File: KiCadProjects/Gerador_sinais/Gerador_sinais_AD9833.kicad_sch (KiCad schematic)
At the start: 18 parts, among them J1 tensoes, J3 sinais analogicos, J4 comunicacao / sinais digitais, J6 pinos de prova, SW1 botao_forma_onda, SW2 botao_incremento_freq, SW3 botao_decremento_freq, SW4 botao_save_Rgain, SW5 botao_aumenta_Rgain, SW6 botao_diminui_Rgain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

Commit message: Atualização das informações da página do esquemático
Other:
- title: Gerador de sinais AD9833 ganho BIA -> Gerador de sinais AD9833
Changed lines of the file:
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@@
   (paper "A4")
   (title_block
-    (title "Gerador de sinais AD9833 ganho BIA")
-    (date "2023-04-19")
+    (title "Gerador de sinais AD9833")
+    (date "2023-07-12")
     (rev "v01")
     (company "EITduino")
     (comment 1 "Autor: Gustavo Pinheiro")
     (comment 2 "placa de face simples 90x100 mm")
-    (comment 3 "Gerador de sinais implementado para a balanca de bioimpedancia")
+    (comment 3 "Gerador de sinais")
     (comment 4 "potenciometro digital: x9c104 (100k)")
-    (comment 5 "controle do pot dig: https://drive.google.com/drive/folders/1YxCH3byESSoGbQtQ7U2HApApApZmV-oW")
   )
   (junction (at 128.905 53.34) (diameter 0) (color 0 0 0 0)

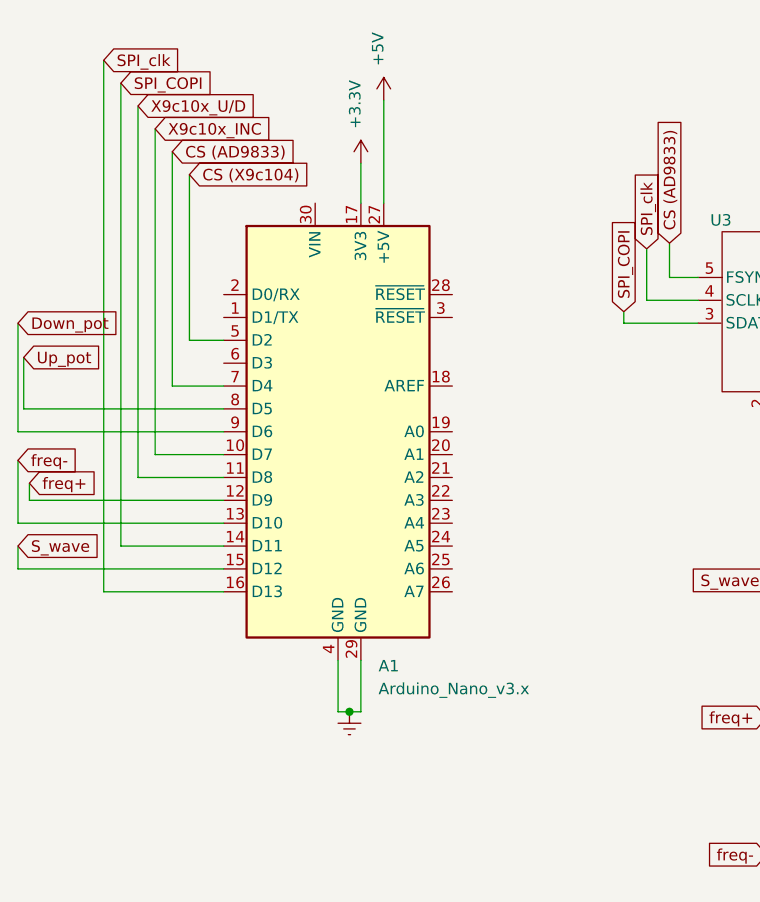
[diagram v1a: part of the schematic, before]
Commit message: Conexão do arduino nano ao I2c 1
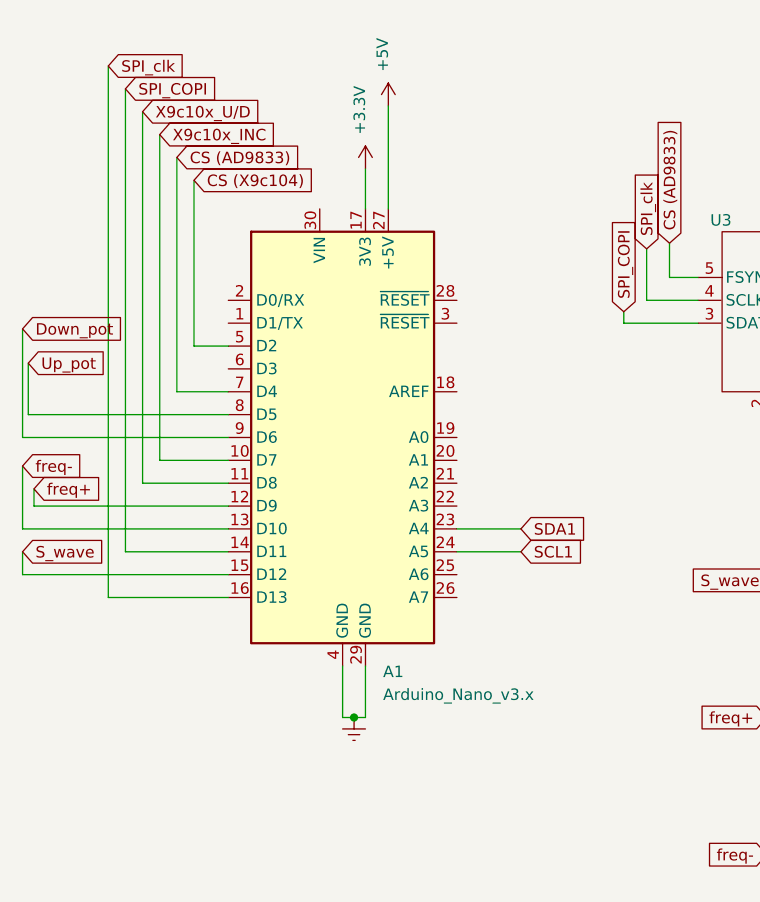
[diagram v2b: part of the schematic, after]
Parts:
- Rpulldown_pot1: footprint (none) -> Resistor_THT:R_Axial_DIN0204_L3.6mm_D1.6mm_P5.08mm_Horizontal
- SW1, SW2, SW3, SW4, SW5, SW6: footprint (none) -> push_button_2_pin:SW_BUTT-2
- U2: footprint (none) -> X9c10X_module:X9c10X_module
- U3: footprint (none) -> AD9833_module:AD9833_module
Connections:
- net SCL1: now also A1.24 (A5)
- net SDA1: now also A1.23 (A4)
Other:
- moved on the sheet: A1

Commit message: mudancas comunicacao SPI
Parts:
- removed Rpulldown_pot1: 10k, Resistor_THT:R_Axial_DIN0204_L3.6mm_D1.6mm_P5.08mm_Horizontal, symbol Device:R
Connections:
- net +3.3V: no longer A1.17 (3V3)
- net +5V: no longer SW4.1
- net CS (X9c104): no longer SW4.2
- net Earth: now also SW4.2
- net storage_R: now reaches A1.6 (D3)
- net storage_R: now also SW4.1

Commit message: Atribuição dos footprints
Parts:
- U1: footprint footprints:N_8_ADI -> AD828AN:N_8_ADI
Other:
- moved on the sheet: A1

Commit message: Atribuição dos footprints
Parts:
- U1: footprint AD828AN:N_8_ADI -> AD828:N_8_ADI
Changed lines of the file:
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@@
       (effects (font (size 1.524 1.524)))
     )
-    (property "Footprint" "AD828AN:N_8_ADI" (at 177.165 45.085 0)
+    (property "Footprint" "AD828:N_8_ADI" (at 177.165 45.085 0)
       (effects (font (size 1.27 1.27) italic) hide)
     )

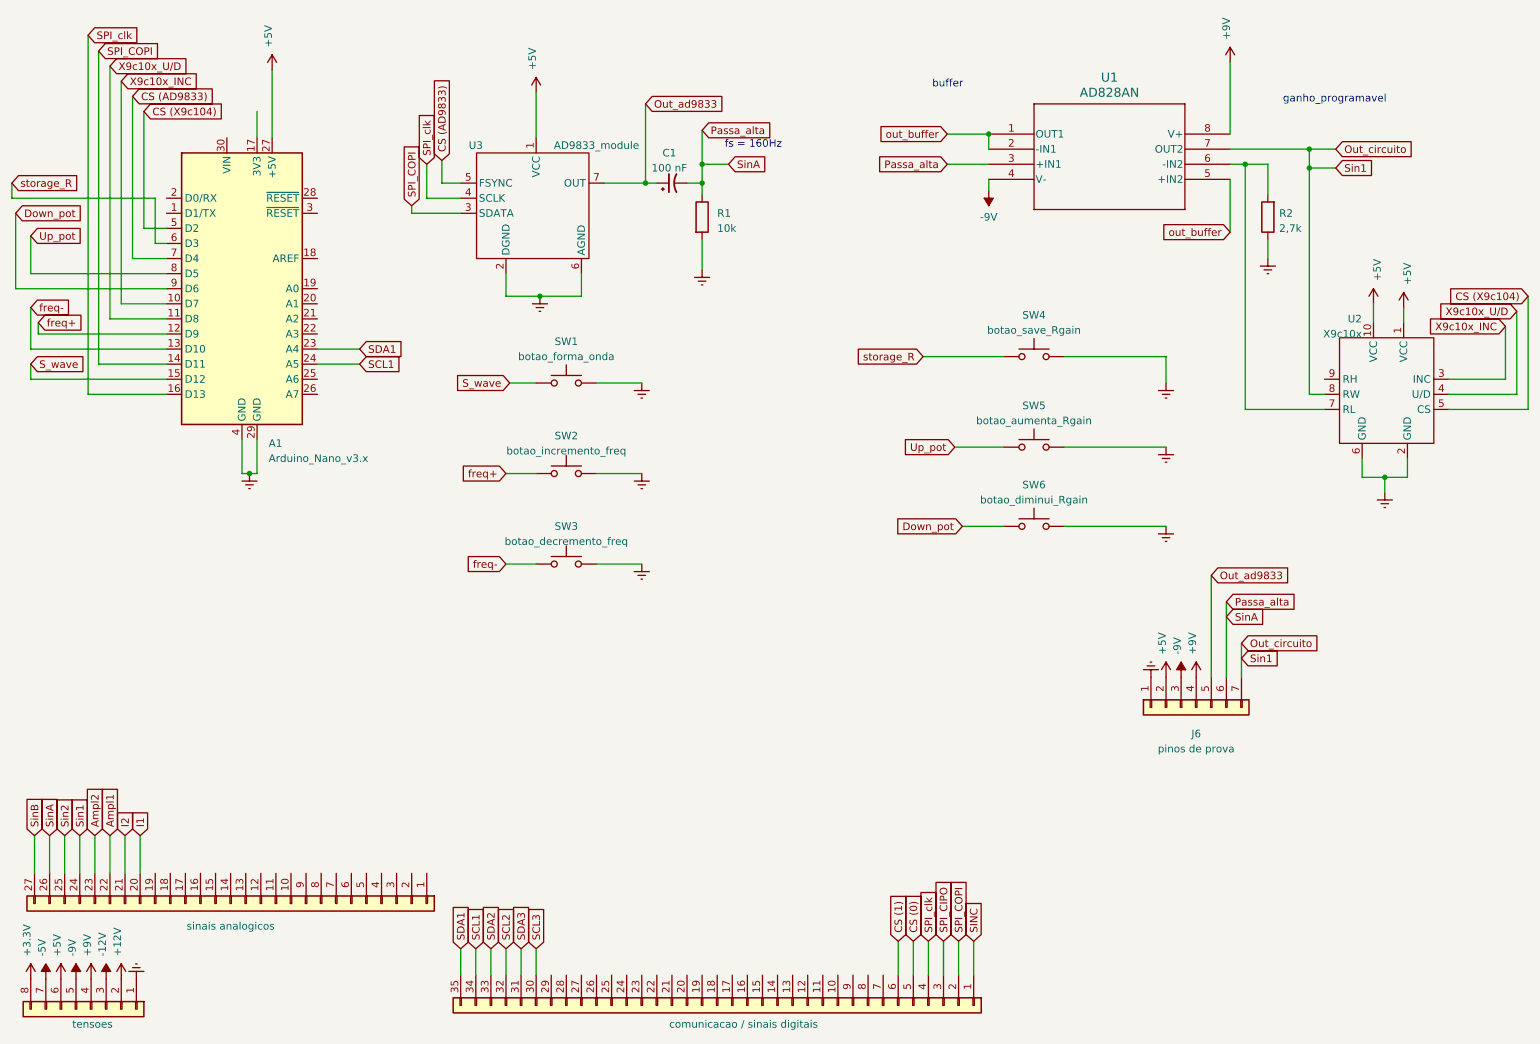
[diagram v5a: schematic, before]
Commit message: Esquema PCB
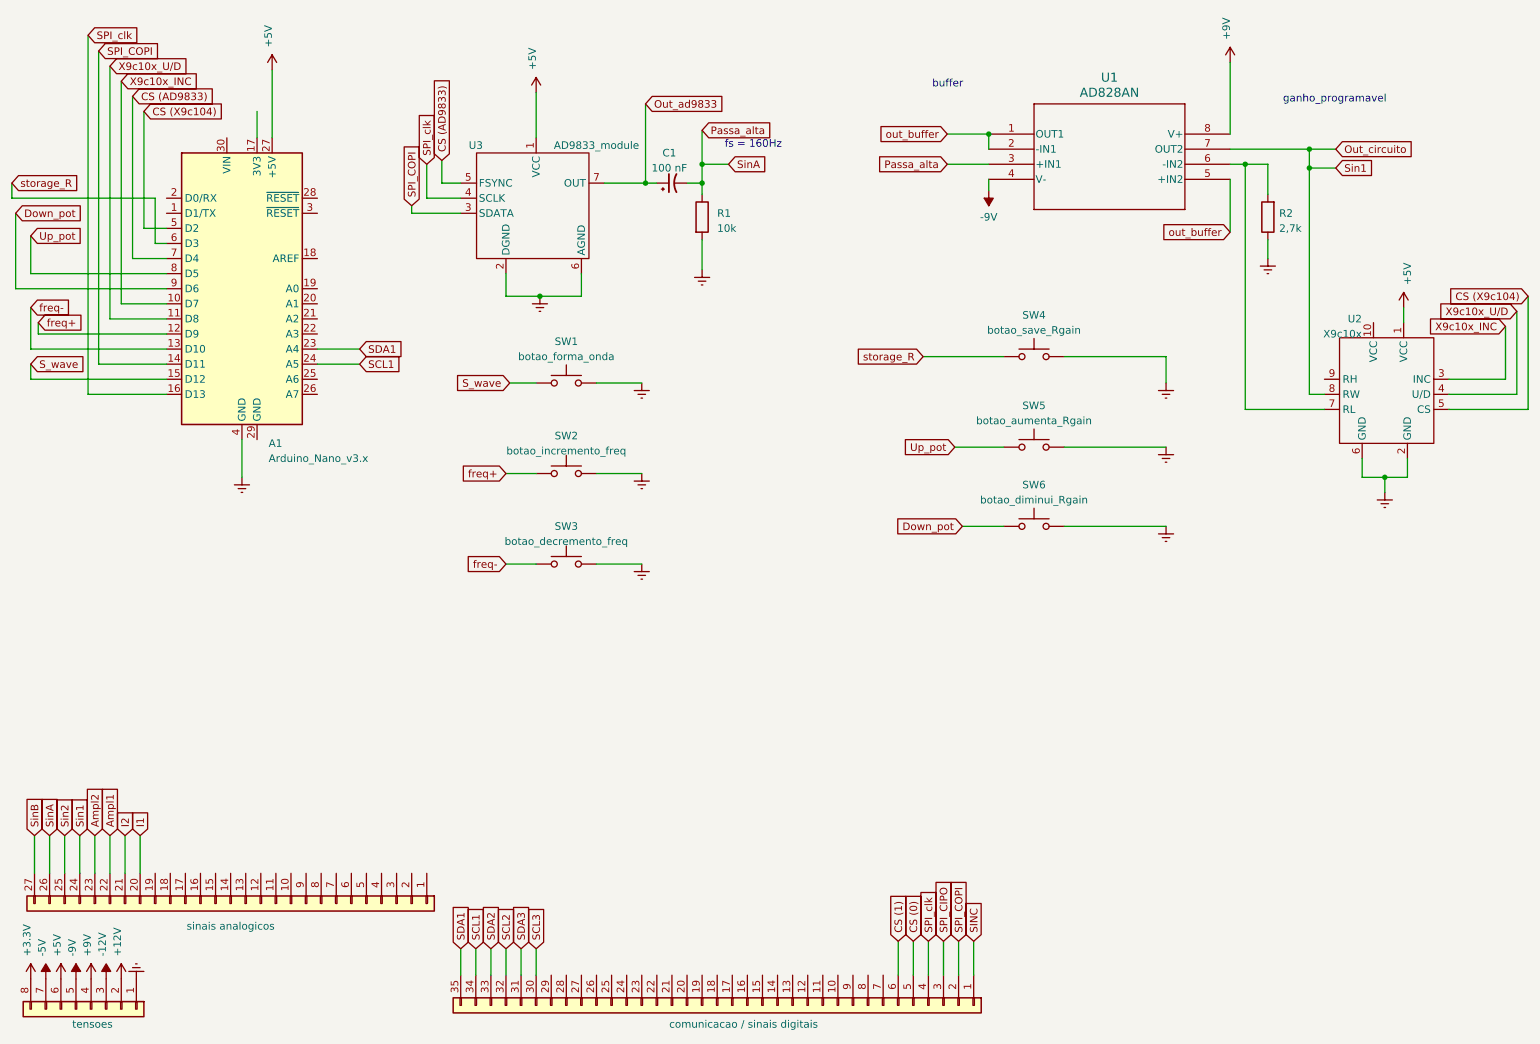
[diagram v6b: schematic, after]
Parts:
- removed J6: pinos de prova, Connector_PinHeader_2.54mm:PinHeader_1x07_P2.54mm_Horizontal, symbol Connector_Generic:Conn_01x07
- C1: footprint Capacitor_THT:CP_Radial_D4.0mm_P1.50mm -> Capacitor_THT:CP_Radial_D5.0mm_P2.50mm
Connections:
- net +5V: no longer U2.10 (VCC)
- net Earth: no longer A1.29 (GND)
